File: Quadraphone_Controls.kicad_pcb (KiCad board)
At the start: 2 copper layers, 60 x 110 mm, 17 parts, among them J1 Conn_01x10_Female, J10 Pitch_In, J11 Mix_Out, J2 Conn_01x10_Female, J3 Conn_01x10_Female, J4 Conn_01x10_Female, J5 PWM_CV, J6 LFO_IN, J7 PWM_CV_In, J8 Synch_Signal_In, J9 Freq_Mod_In, SW1 Synch_Type, SW2 Output_Type

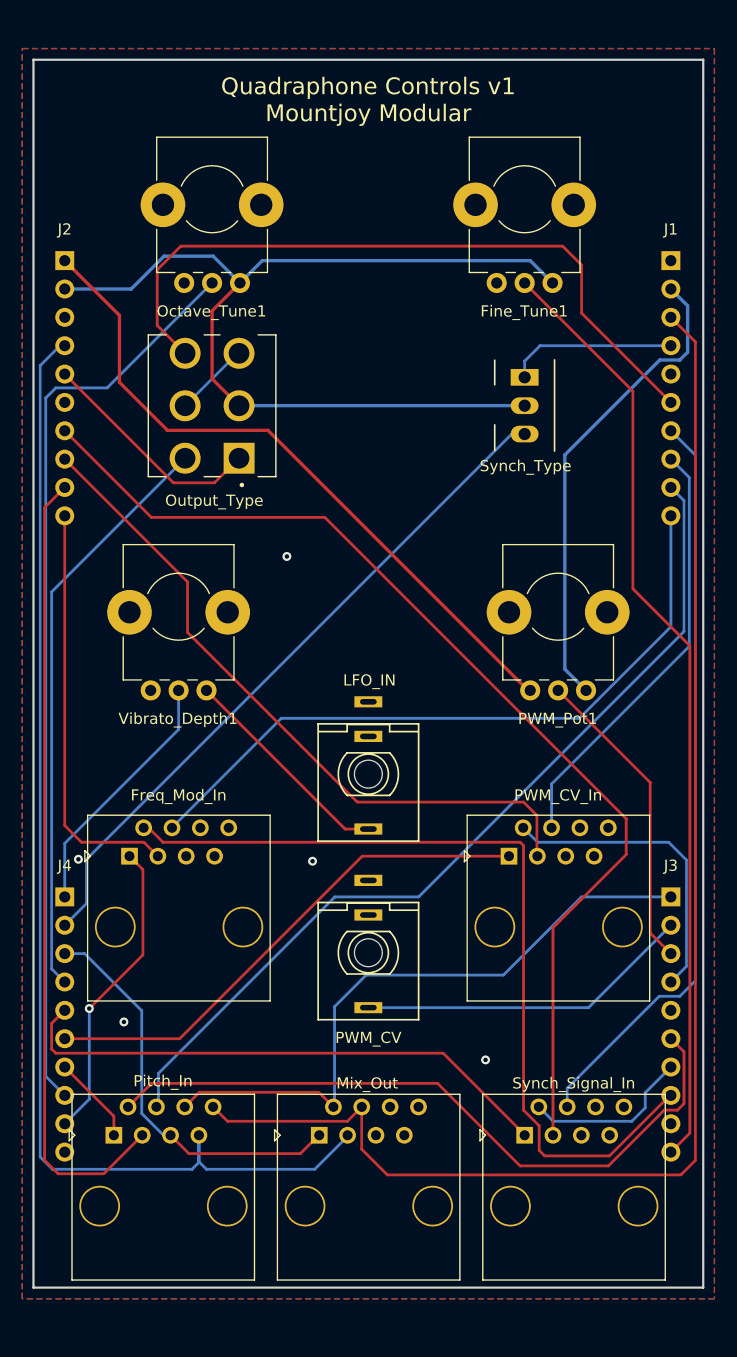
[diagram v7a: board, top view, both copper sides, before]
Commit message: Updates for v2 on control board
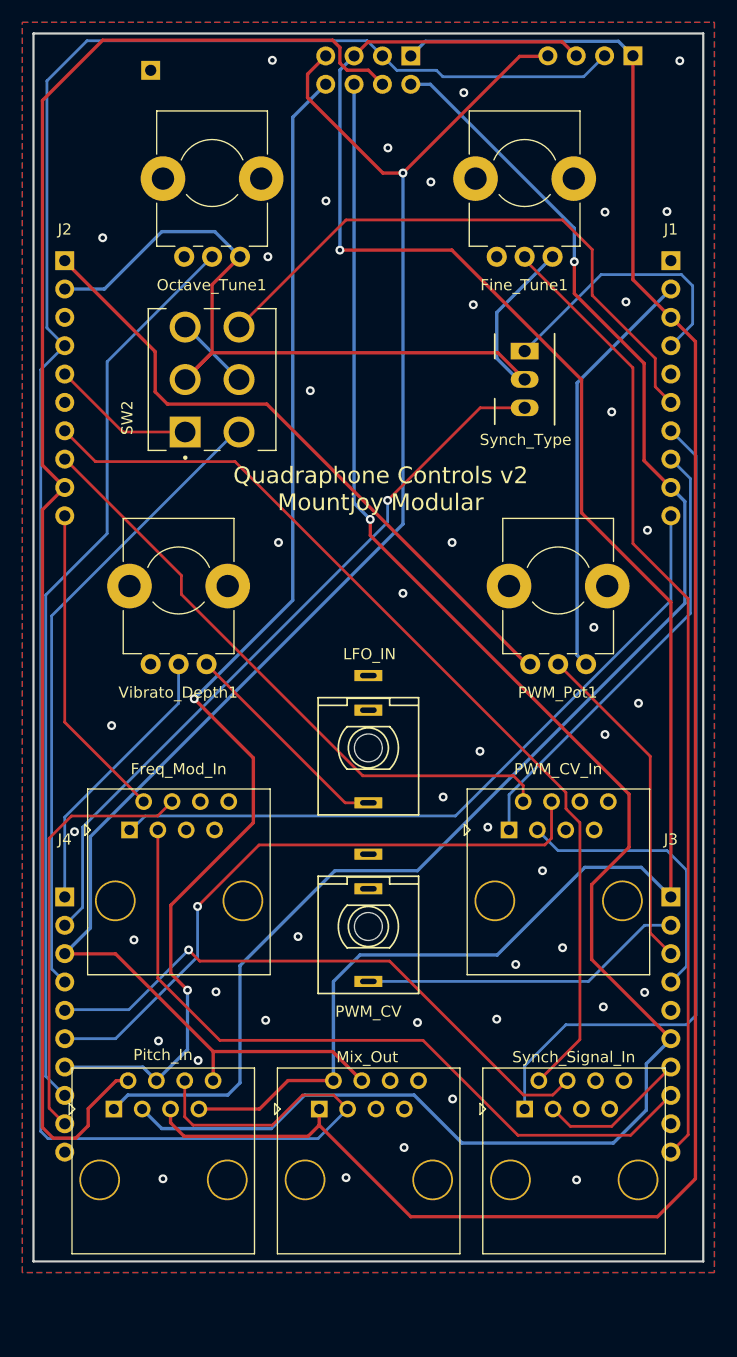
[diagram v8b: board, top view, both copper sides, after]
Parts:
- added J12: Conn_02x04_Top_Bottom, Connector_PinSocket_2.54mm:PinSocket_2x04_P2.54mm_Vertical, B.Cu at (83.8, 44.7)
- added J13: Conn_01x04_Male, Connector_PinHeader_2.54mm:PinHeader_1x04_P2.54mm_Vertical, B.Cu at (103.7, 44.6)
- added J14: Conn_01x01_Male, Connector_PinHeader_2.54mm:PinHeader_1x01_P2.54mm_Vertical, B.Cu at (60.5, 46.0)
- SW2: footprint Custom_Footprints:SW_100DP3T1B1M2QEH -> Custom_Footprints:100DP6T1B1M2QE_ON_ON_ON
- moved SW1 2.35 mm to (94.0, 71.1)
- moved Fine_Tune1 2.35 mm to (94.0, 55.1)
- moved Octave_Tune1 2.35 mm to (66.0, 55.1)
- moved J10 2.35 mm to (61.6, 143.7)
- moved J11 2.35 mm to (80.0, 143.7)
- moved J5 2.35 mm to (80.0, 122.7)
- moved J6 2.35 mm to (80.0, 106.7)
- moved J7 2.35 mm to (97.0, 118.7)
- moved J8 2.35 mm to (98.4, 143.7)
- moved J9 2.35 mm to (63.0, 118.7)
- moved PWM_Pot1 2.35 mm to (97.0, 91.7)
- moved SW2 2.35 mm to (66.0, 73.7)
- moved Vibrato_Depth1 2.35 mm to (63.0, 91.7)
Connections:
- J10 pad 1: /V_PER_OCT4 -> /V_PER_OCT1
- J10 pad 2: /V_PER_OCT3 -> /V_PER_OCT2
- J10 pad 3: /V_PER_OCT2 -> /V_PER_OCT3
- J10 pad 4: /V_PER_OCT1 -> /V_PER_OCT4
- J10 pad 5: /MIX_OUT4 -> /MIX_OUT1
- J10 pad 6: /MIX_OUT3 -> /MIX_OUT2
- J10 pad 7: /MIX_OUT2 -> /MIX_OUT3
- J10 pad 8: /MIX_OUT1 -> /MIX_OUT4
- J11 pad 1: /MIX_OUT4 -> /MIX_OUT1
- J11 pad 4: /MIX_OUT1 -> /MIX_OUT4
- J7 pad 1: /PWM_CV4 -> /PWM_CV1
- J7 pad 2: /PWM_CV3 -> /PWM_CV2
- J7 pad 3: /PWM_CV2 -> /PWM_CV3
- J7 pad 4: /PWM_CV1 -> /PWM_CV4
- J8 pad 1: /SYNCH_SIGNAL4 -> /SYNCH_SIGNAL1
- J8 pad 2: /SYNCH_SIGNAL3 -> /SYNCH_SIGNAL2
- J8 pad 3: /SYNCH_SIGNAL2 -> /SYNCH_SIGNAL3
- J8 pad 4: /SYNCH_SIGNAL1 -> /SYNCH_SIGNAL4
- J9 pad 1: /FREQ_MOD4 -> /FREQ_MOD1
- J9 pad 2: /FREQ_MOD3 -> /FREQ_MOD2
- J9 pad 3: /FREQ_MOD2 -> /FREQ_MOD3
- J9 pad 4: /FREQ_MOD1 -> /FREQ_MOD4
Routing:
- net /MIX_OUT3: track 57.6 -> 172.5 mm, vias 0 -> 1
- net /MIX_OUT4: track 36.3 -> 149.5 mm, vias 0 -> 1
- net /V_PER_OCT4: track 7.93 -> 109.9 mm, vias 0 -> 2
- net /V_PER_OCT3: track 62.4 -> 157.6 mm, vias 0 -> 1
- net /MIX_OUT2: track 108.5 -> 197.9 mm
- net /V_PER_OCT2: track 71.7 -> 139.9 mm
- net /V_PER_OCT1: track 79.9 -> 133.8 mm, vias 0 -> 1
- net /MIX_OUT1: track 126.0 -> 179.4 mm
- net /FREQ_MOD4: track 27.4 -> 38.5 mm, vias 1 -> 0
- net /PWM_CV4: track 46.6 -> 57.0 mm, vias 0 -> 1
- net /SAW_SW: track 63.7 -> 53.3 mm
- net /FREQ_MOD3: track 76.8 -> 66.6 mm
- net /SYNCH_SIGNAL2: track 95.8 -> 86.2 mm
- net /HARD_SYNCH_SW: track 15.1 -> 24.5 mm
- net /FREQ_MOD2: track 37.2 -> 28.5 mm
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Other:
- board text added: "1"
- board text added: "4"
- board text added: "GND"
- board text added: "OUT"
- board text added: "Quadraphone Controls v2 Mountjoy Modular"
- board text added: "V/OCT"
- board text removed: "Quadraphone Controls v1 Mountjoy Modular"
